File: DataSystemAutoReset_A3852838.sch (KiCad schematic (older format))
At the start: 0 parts

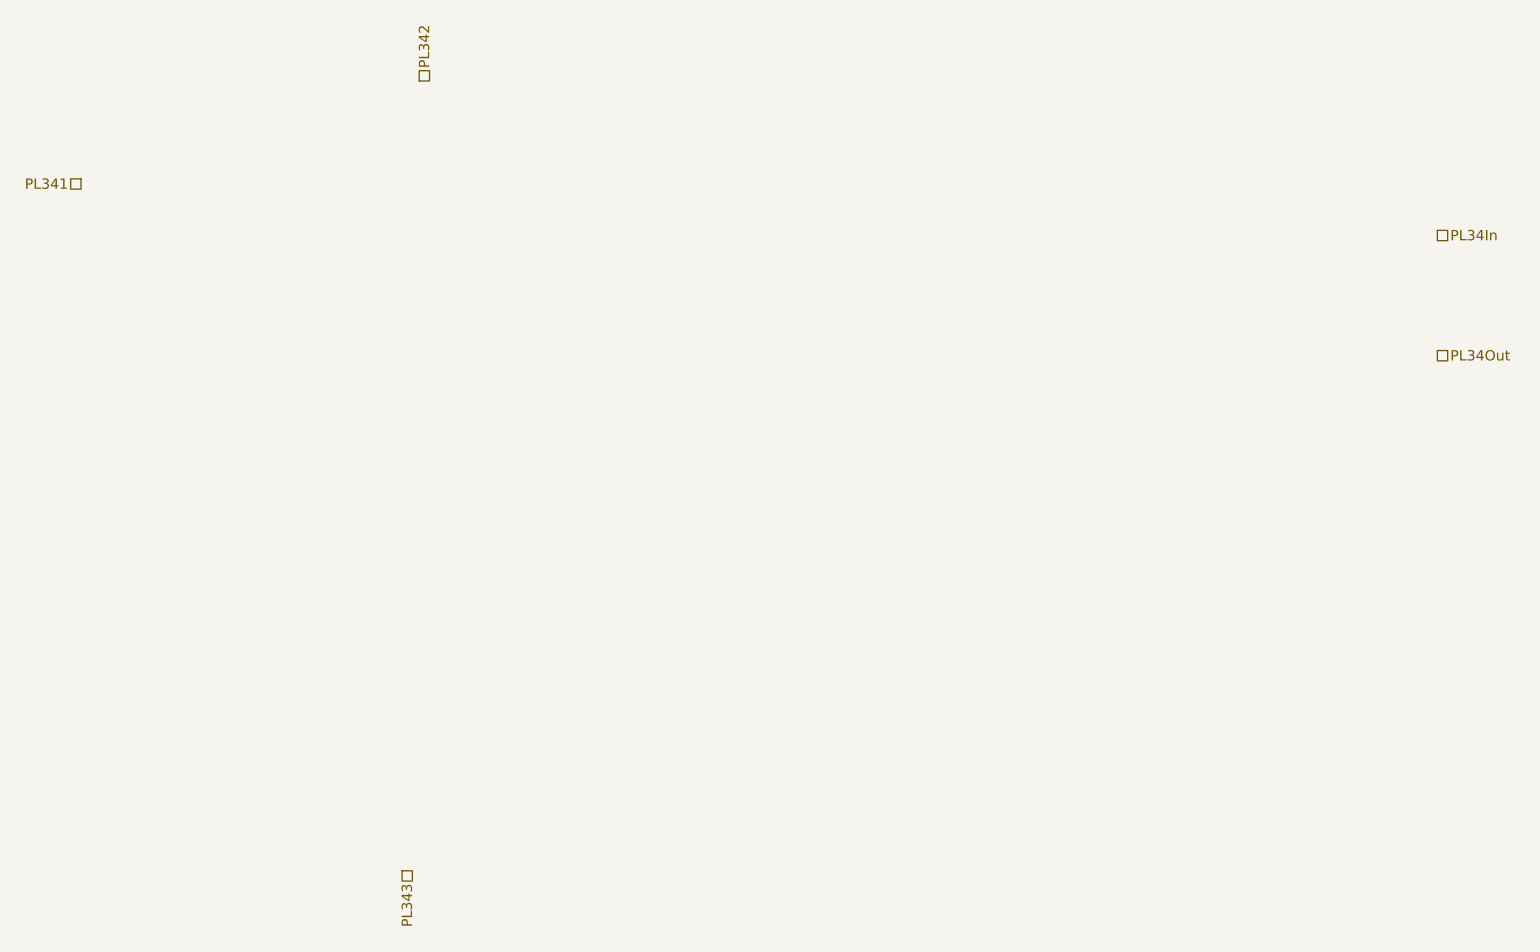
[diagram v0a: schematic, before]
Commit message: added ColumnWiring, DataSystemAutoReset, KVSelection and VacuumInterlock
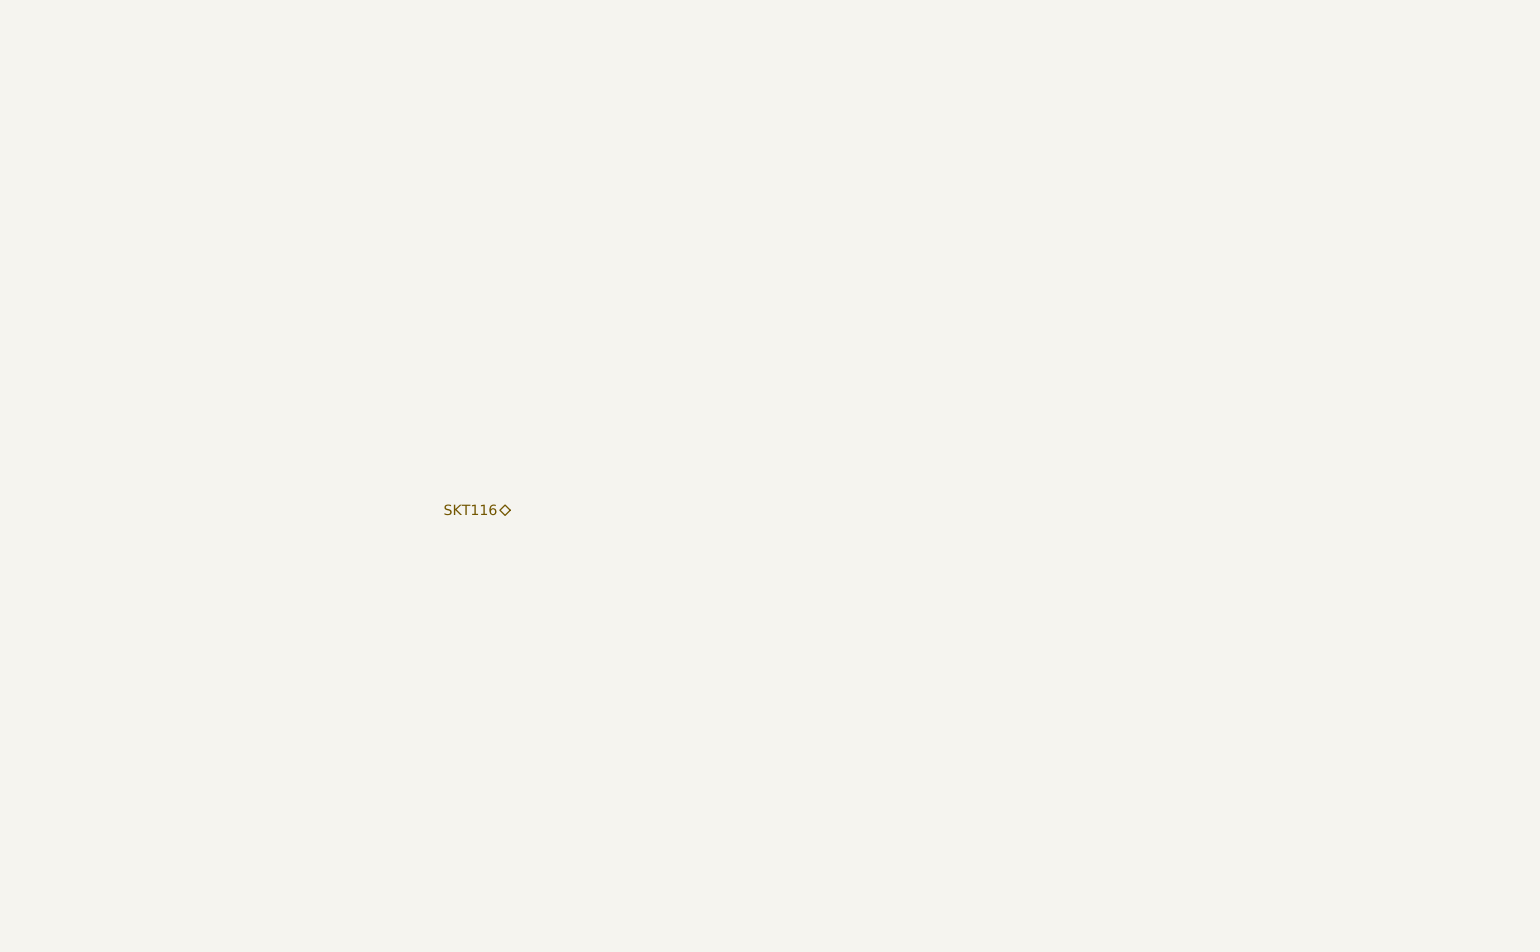
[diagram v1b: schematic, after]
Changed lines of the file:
@@
 $Descr A4 11693 8268
 encoding utf-8
-Sheet 9 25
+Sheet 24 25
 Title ""
 Date ""
@@
 Comment4 ""
 $EndDescr
-Text HLabel 1800 1900 0    60   UnSpc ~ 0
-PL341
-Text HLabel 3800 1300 1    60   UnSpc ~ 0
-PL342
-Text HLabel 3700 5900 3    60   UnSpc ~ 0
-PL343
-Text HLabel 9700 2200 2    60   UnSpc ~ 0
-PL34In
-Text HLabel 9700 2900 2    60   UnSpc ~ 0
-PL34Out
+Text HLabel 4300 3800 0    60   BiDi ~ 0
+SKT116
 $EndSCHEMATC
